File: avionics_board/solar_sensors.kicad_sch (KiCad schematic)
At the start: 4 parts, among them U13 TCA9548APWR

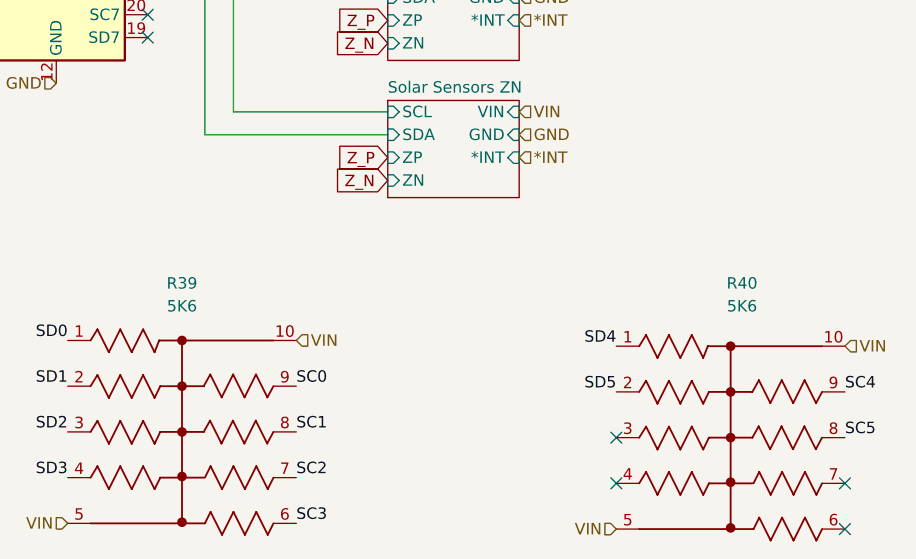
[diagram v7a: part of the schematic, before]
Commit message: SCI AVI and EPS are now consistent
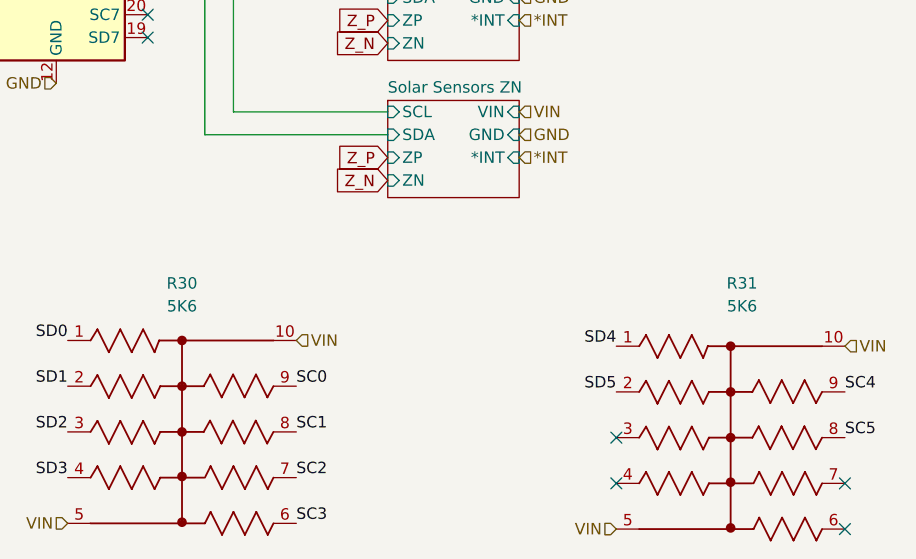
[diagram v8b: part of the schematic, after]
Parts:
- renumbered R39 to R30, R40 to R31
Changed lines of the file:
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@@
 		(on_board yes)
 		(dnp no)
-		(property "Reference" "R39"
+		(property "Reference" "R30"
 			(at 99.06 135.89 0)
 			(effects
@@
 				)
 				(hide yes)
+			)
+		)
+		(property "Manufactorer" ""
+			(at 86.36 142.24 0)
+			(effects
+				(font
+					(size 1.27 1.27)
+				)
+			)
+		)
+		(property "Sim.Pins" ""
+			(at 86.36 142.24 0)
+			(effects
+				(font
+					(size 1.27 1.27)
+				)
 			)
 		)
@@
 			(project ""
 				(path "/f6cc00ab-17f1-4973-862f-7ac95fe70668/472a2b3c-f2e4-44b5-9587-658c9c0c9365"
-					(reference "R39")
+					(reference "R30")
 					(unit 1)
 				)
@@
 		(on_board yes)
 		(dnp no)
-		(property "Reference" "R40"
+		(property "Reference" "R31"
 			(at 161.29 135.89 0)
 			(effects
@@
 				)
 				(hide yes)
+			)
+		)
+		(property "Manufactorer" ""
+			(at 147.32 142.875 0)
+			(effects
+				(font
+					(size 1.27 1.27)
+				)
+			)
+		)
+		(property "Sim.Pins" ""
+			(at 147.32 142.875 0)
+			(effects
+				(font
+					(size 1.27 1.27)
+				)
 			)
 		)
@@
 			(project "AVIONICS_BOARD"
 				(path "/f6cc00ab-17f1-4973-862f-7ac95fe70668/472a2b3c-f2e4-44b5-9587-658c9c0c9365"
-					(reference "R40")
+					(reference "R31")
 					(unit 1)
 				)
@@
 			)
 		)
+		(property "Manufactorer" ""
+			(at 92.075 59.055 0)
+			(effects
+				(font
+					(size 1.27 1.27)
+				)
+			)
+		)
+		(property "Sim.Pins" ""
+			(at 92.075 59.055 0)
+			(effects
+				(font
+					(size 1.27 1.27)
+				)
+			)
+		)
 		(pin "1"
 		)
@@
 			)
 		)
+		(property "Manufactorer" ""
+			(at 85.09 88.265 0)
+			(effects
+				(font
+					(size 1.27 1.27)
+				)
+			)
+		)
+		(property "Sim.Pins" ""
+			(at 85.09 88.265 0)
+			(effects
+				(font
+					(size 1.27 1.27)
+				)
+			)
+		)
